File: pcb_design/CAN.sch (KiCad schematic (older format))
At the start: 5 parts

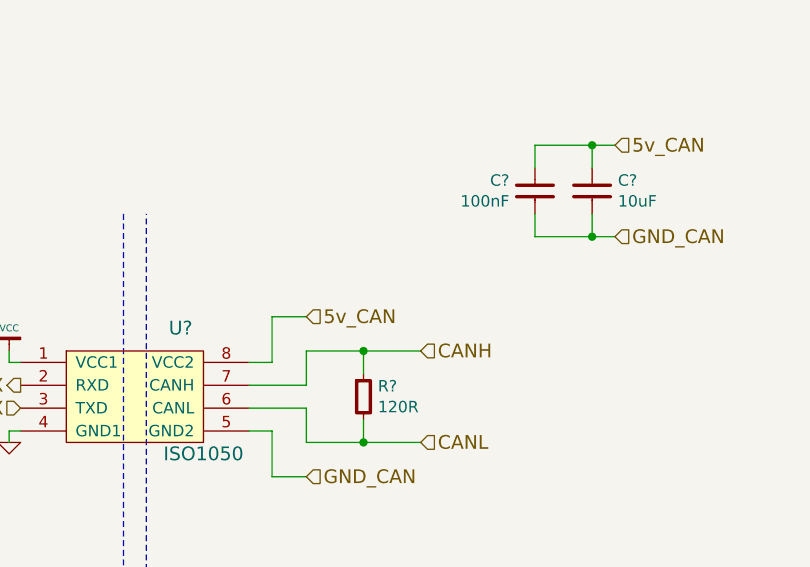
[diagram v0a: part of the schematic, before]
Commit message: Updated MCU sheet to comply with VESC 6 pinout. Added 5v analog inputs and updated some labels
Signed-off-by: Marcos Chaparro <mchaparro@paltatech.com>
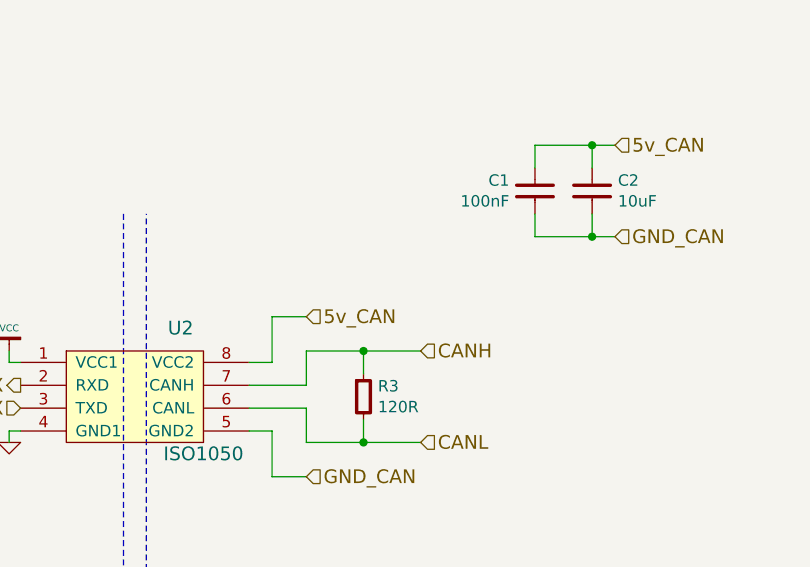
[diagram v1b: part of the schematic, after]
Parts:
- gave numbers to parts that had none: 4
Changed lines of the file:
@@
 $Descr A4 11693 8268
 encoding utf-8
-Sheet 3 10
+Sheet 3 12
 Title "BLDC Driver 4.11"
 Date "21 aug 2015"
@@
 $EndDescr
 $Comp
-L GND-RESCUE-BLDC_4 #PWR025
+L GND-RESCUE-BLDC_4 #PWR021
 U 1 1 53F59F97
 P 4950 4250
-F 0 "#PWR025" H 4950 4250 30  0001 C CNN
+F 0 "#PWR021" H 4950 4250 30  0001 C CNN
 F 1 "GND" H 4950 4180 30  0001 C CNN
 F 2 "" H 4950 4250 60  0000 C CNN
@@
 $EndComp
 $Comp
-L VCC #PWR026
+L VCC #PWR022
 U 1 1 53F59F9D
 P 4950 3850
-F 0 "#PWR026" H 4950 3950 30  0001 C CNN
+F 0 "#PWR022" H 4950 3950 30  0001 C CNN
 F 1 "VCC" H 4950 3950 30  0000 C CNN
 F 2 "" H 4950 3850 60  0001 C CNN
@@
 $EndComp
 $Comp
-L VCC #PWR027
+L VCC #PWR023
 U 1 1 53F59FAA
 P 4000 3850
-F 0 "#PWR027" H 4000 3950 30  0001 C CNN
+F 0 "#PWR023" H 4000 3950 30  0001 C CNN
 F 1 "VCC" H 4000 3950 30  0000 C CNN
 F 2 "" H 4000 3850 60  0001 C CNN
@@
 $EndComp
 $Comp
-L GND-RESCUE-BLDC_4 #PWR028
+L GND-RESCUE-BLDC_4 #PWR024
 U 1 1 53F59FB0
 P 4000 4250
-F 0 "#PWR028" H 4000 4250 30  0001 C CNN
+F 0 "#PWR024" H 4000 4250 30  0001 C CNN
 F 1 "GND" H 4000 4180 30  0001 C CNN
 F 2 "" H 4000 4250 60  0000 C CNN
@@
 CANL
 $Comp
-L ISO1050 U?
+L ISO1050 U2
 U 1 1 5886CCC8
 P 5500 4050
-F 0 "U?" H 5700 4350 60  0000 C CNN
+F 0 "U2" H 5700 4350 60  0000 C CNN
 F 1 "ISO1050" H 5800 3800 60  0000 C CNN
 F 2 "paltatech:SO8-ISO1050" H 5650 3850 60  0001 C CNN
@@
 $EndComp
 $Comp
-L R-0603 R?
+L R-0603 R3
 U 1 1 588777AE
 P 6500 4050
-F 0 "R?" H 6563 4096 50  0000 L CNN
+F 0 "R3" H 6563 4096 50  0000 L CNN
 F 1 "120R" H 6563 4005 50  0000 L CNN
 F 2 "IPC7351-Nominal:RESC1608X50" H 6500 4050 50  0001 C CNN
@@
 $EndComp
 $Comp
-L C-0805 C?
+L C-0805 C2
 U 1 1 58877A76
 P 7500 3150
-F 0 "C?" H 7613 3196 50  0000 L CNN
+F 0 "C2" H 7613 3196 50  0000 L CNN
 F 1 "10uF" H 7613 3105 50  0000 L CNN
 F 2 "IPC7351-Nominal:CAPC2012X70" H 7500 3150 50  0001 C CNN
@@
 $EndComp
 $Comp
-L C-0603 C?
+L C-0603 C1
 U 1 1 58877AC7
 P 7250 3150
-F 0 "C?" H 7362 3196 50  0000 L CNN
+F 0 "C1" H 7362 3196 50  0000 L CNN
 F 1 "100nF" H 7362 3105 50  0000 L CNN
 F 2 "IPC7351-Nominal:CAPC1608X55" H 7250 3150 50  0001 C CNN

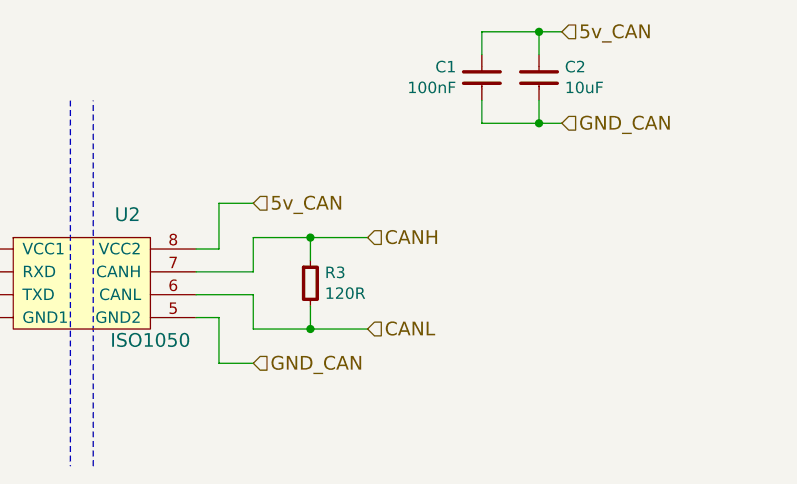
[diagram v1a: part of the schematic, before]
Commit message: Components placement, 3D models, updated some footprints to nominal IPC type
Signed-off-by: Marcos Chaparro <mchaparro@paltatech.com>
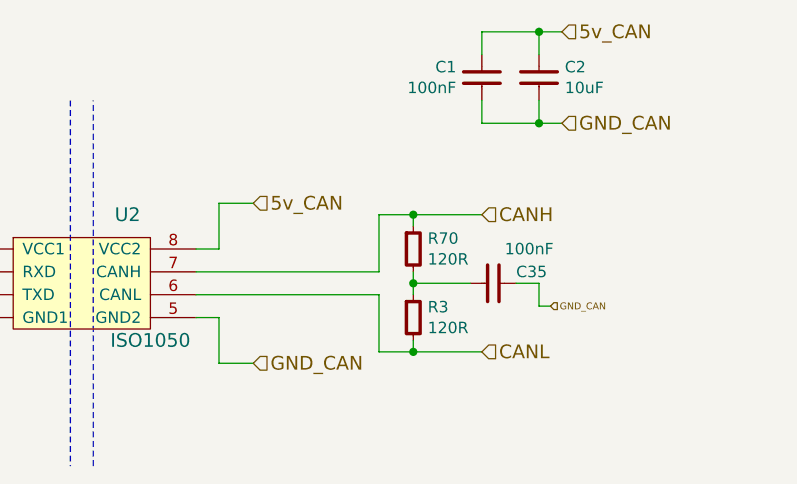
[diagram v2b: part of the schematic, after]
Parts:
- added C35: 100nF, IPC7351-Nominal:CAPC1608X55, symbol C-0603
- added R70: 120R, IPC7351-Nominal:RESC1608X50, symbol R-0603
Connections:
- net CANH: now also R70.1; no longer R3.1
- net GND_CAN: now also C35.1
- new net: C35.2, R3.1, R70.2
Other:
- moved on the sheet: R3
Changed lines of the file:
@@
 $EndDescr
 $Comp
-L GND-RESCUE-BLDC_4 #PWR021
+L GND-RESCUE-BLDC_4 #PWR21
 U 1 1 53F59F97
 P 4950 4250
-F 0 "#PWR021" H 4950 4250 30  0001 C CNN
+F 0 "#PWR21" H 4950 4250 30  0001 C CNN
 F 1 "GND" H 4950 4180 30  0001 C CNN
 F 2 "" H 4950 4250 60  0000 C CNN
@@
 $EndComp
 $Comp
-L VCC #PWR022
+L VCC #PWR20
 U 1 1 53F59F9D
 P 4950 3850
-F 0 "#PWR022" H 4950 3950 30  0001 C CNN
+F 0 "#PWR20" H 4950 3950 30  0001 C CNN
 F 1 "VCC" H 4950 3950 30  0000 C CNN
 F 2 "" H 4950 3850 60  0001 C CNN
@@
 $EndComp
 $Comp
-L VCC #PWR023
+L VCC #PWR18
 U 1 1 53F59FAA
 P 4000 3850
-F 0 "#PWR023" H 4000 3950 30  0001 C CNN
+F 0 "#PWR18" H 4000 3950 30  0001 C CNN
 F 1 "VCC" H 4000 3950 30  0000 C CNN
 F 2 "" H 4000 3850 60  0001 C CNN
@@
 $EndComp
 $Comp
-L GND-RESCUE-BLDC_4 #PWR024
+L GND-RESCUE-BLDC_4 #PWR19
 U 1 1 53F59FB0
 P 4000 4250
-F 0 "#PWR024" H 4000 4250 30  0001 C CNN
+F 0 "#PWR19" H 4000 4250 30  0001 C CNN
 F 1 "GND" H 4000 4180 30  0001 C CNN
 F 2 "" H 4000 4250 60  0000 C CNN
@@
 Text HLabel 5000 4100 0    60   Input ~ 0
 CAN_TX
-Text HLabel 6750 3850 2    60   Input ~ 0
+Text HLabel 7250 3750 2    60   Input ~ 0
 CANH
-Text HLabel 6750 4250 2    60   Input ~ 0
+Text HLabel 7250 4350 2    60   Input ~ 0
 CANL
 $Comp
@@
 L R-0603 R3
 U 1 1 588777AE
-P 6500 4050
-F 0 "R3" H 6563 4096 50  0000 L CNN
-F 1 "120R" H 6563 4005 50  0000 L CNN
-F 2 "IPC7351-Nominal:RESC1608X50" H 6500 4050 50  0001 C CNN
-F 3 "" H 6500 4100 60  0000 C CNN
-F 4 "RES SMD 1k 5% [0603]" H 7250 4600 60  0001 C CNN "BOM"
-	1    6500 4050
+P 6950 4200
+F 0 "R3" H 7013 4246 50  0000 L CNN
+F 1 "120R" H 7013 4155 50  0000 L CNN
+F 2 "IPC7351-Nominal:RESC1608X50" H 6950 4200 50  0001 C CNN
+F 3 "" H 6950 4250 60  0000 C CNN
+F 4 "RES SMD 1k 5% [0603]" H 7700 4750 60  0001 C CNN "BOM"
+	1    6950 4200
 	1    0    0    -1
 $EndComp
@@
 $EndComp
 Wire Wire Line
-	6250 4250 6750 4250
-Wire Wire Line
-	6250 4250 6250 4100
-Wire Wire Line
-	6250 4100 6000 4100
-Connection ~ 6500 4250
-Wire Wire Line
-	6000 4000 6250 4000
-Wire Wire Line
-	6250 4000 6250 3850
-Wire Wire Line
-	6250 3850 6750 3850
-Connection ~ 6500 3850
-Wire Wire Line
 	4950 3850 4950 3900
 Wire Wire Line
@@
 Wire Wire Line
 	4950 4200 5000 4200
-Wire Wire Line
-	6500 3950 6500 3850
-Wire Wire Line
-	6500 4150 6500 4250
 Wire Wire Line
 	7500 3050 7500 2950
@@
 Text Notes 1200 1700 0    300  ~ 60
 ISOLATED CAN BUS DRIVER
+$Comp
+L R-0603 R70
+U 1 1 588FD082
+P 6950 3900
+F 0 "R70" H 7013 3946 50  0000 L CNN
+F 1 "120R" H 7013 3855 50  0000 L CNN
+F 2 "IPC7351-Nominal:RESC1608X50" H 6950 3900 50  0001 C CNN
+F 3 "" H 6950 3950 60  0000 C CNN
+F 4 "RES SMD 1k 5% [0603]" H 7700 4450 60  0001 C CNN "BOM"
+	1    6950 3900
+	1    0    0    -1
+$EndComp
+Wire Wire Line
+	6000 4000 6800 4000
+Wire Wire Line
+	6800 4000 6800 3750
+Wire Wire Line
+	6800 3750 7250 3750
+Wire Wire Line
+	6950 3800 6950 3750
+Connection ~ 6950 3750
+$Comp
+L C-0603 C35
+U 1 1 588FD468
+P 7300 4050
+F 0 "C35" V 7350 4150 50  0000 L CNN
+F 1 "100nF" V 7450 4100 50  0000 L CNN
+F 2 "IPC7351-Nominal:CAPC1608X55" H 7300 4050 50  0001 C CNN
+F 3 "" H 7290 4025 60  0000 C CNN
+F 4 "CAP MLCC 100pF C0G 50V 5% [0603]" H 8100 4600 60  0001 C CNN "BOM"
+	1    7300 4050
+	0    1    -1   0
+$EndComp
+Wire Wire Line
+	7200 4050 6950 4050
+Wire Wire Line
+	6950 4000 6950 4100
+Connection ~ 6950 4050
+Wire Wire Line
+	6000 4100 6800 4100
+Wire Wire Line
+	6800 4100 6800 4350
+Wire Wire Line
+	6800 4350 7250 4350
+Wire Wire Line
+	6950 4350 6950 4300
+Connection ~ 6950 4350
+Wire Wire Line
+	7400 4050 7500 4050
+Wire Wire Line
+	7500 4050 7500 4150
+Text HLabel 7550 4150 2    30   Input ~ 0
+GND_CAN
+Wire Wire Line
+	7500 4150 7550 4150
 $EndSCHEMATC

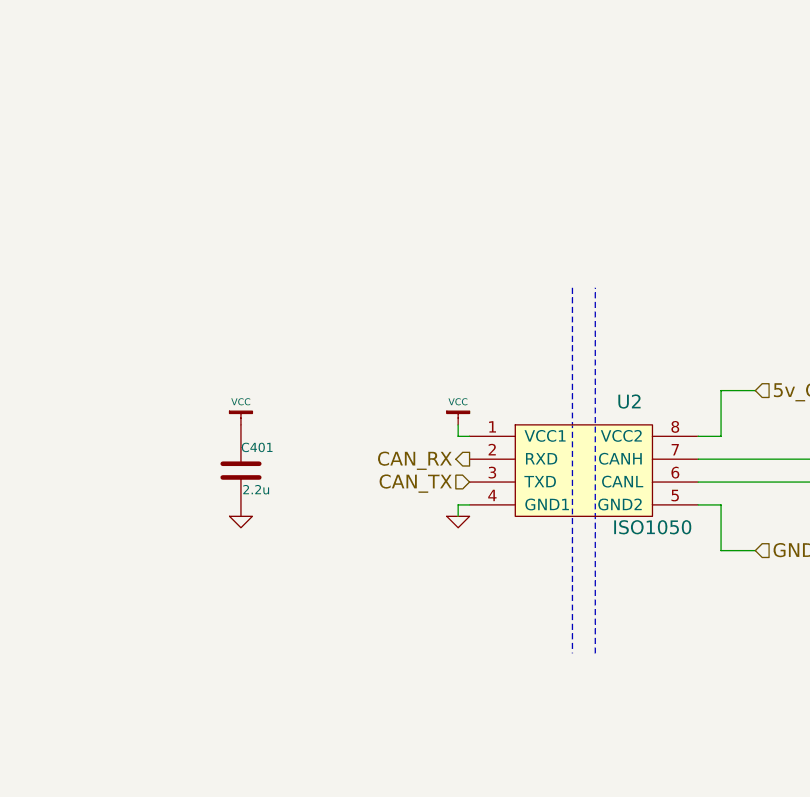
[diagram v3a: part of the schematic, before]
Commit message: Added lp filters, fuses, tvs and power symbols
Signed-off-by: Marcos Chaparro <mchaparro@paltatech.com>
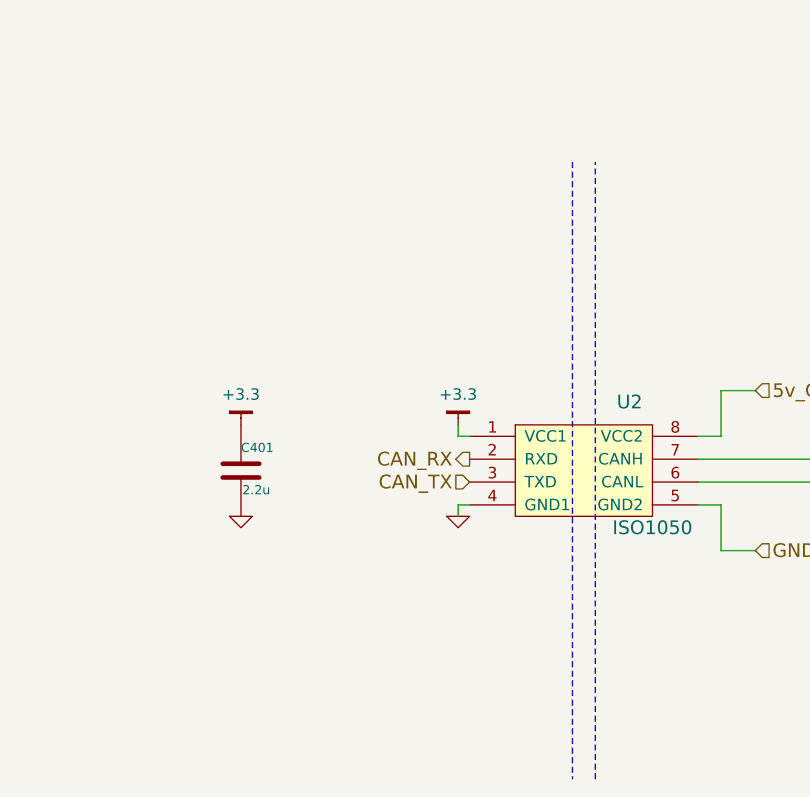
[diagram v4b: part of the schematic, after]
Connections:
- net VCC renamed +3.3
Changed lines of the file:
@@
-$EndComp
-$Comp
-L VCC #PWR23
-U 1 1 53F59F9D
-P 4950 3850
-F 0 "#PWR23" H 4950 3950 30  0001 C CNN
-F 1 "VCC" H 4950 3950 30  0000 C CNN
-F 2 "" H 4950 3850 60  0001 C CNN
-F 3 "" H 4950 3850 60  0001 C CNN
-	1    4950 3850
-	1    0    0    -1
 $EndComp
 $Comp
@@
 F 3 "" H 4000 4050 60  0000 C CNN
 	1    4000 4050
-	1    0    0    -1
-$EndComp
-$Comp
-L VCC #PWR21
-U 1 1 53F59FAA
-P 4000 3850
-F 0 "#PWR21" H 4000 3950 30  0001 C CNN
-F 1 "VCC" H 4000 3950 30  0000 C CNN
-F 2 "" H 4000 3850 60  0001 C CNN
-F 3 "" H 4000 3850 60  0001 C CNN
-	1    4000 3850
 	1    0    0    -1
 $EndComp
@@
 Wire Wire Line
 	6100 3900 6000 3900
-Wire Notes Line
-	5450 3250 5450 4850
-Wire Notes Line
-	5550 4850 5550 3250
 Text Notes 1200 1700 0    300  ~ 60
 ISOLATED CAN BUS DRIVER
@@
 Wire Wire Line
 	7500 4150 7550 4150
+$Comp
+L +3.3 #PWR?
+U 1 1 588B7BD5
+P 4000 3850
+F 0 "#PWR?" H 0   100 30  0001 C CNN
+F 1 "+3.3" H 4000 3983 50  0000 C CNN
+F 2 "" H 0   50  60  0000 C CNN
+F 3 "" H 0   50  60  0000 C CNN
+	1    4000 3850
+	1    0    0    -1
+$EndComp
+$Comp
+L +3.3 #PWR?
+U 1 1 588B7BFF
+P 4950 3850
+F 0 "#PWR?" H 0   100 30  0001 C CNN
+F 1 "+3.3" H 4950 3983 50  0000 C CNN
+F 2 "" H 0   50  60  0000 C CNN
+F 3 "" H 0   50  60  0000 C CNN
+	1    4950 3850
+	1    0    0    -1
+$EndComp
+Wire Notes Line
+	5450 2700 5450 5400
+Wire Notes Line
+	5550 5400 5550 2700
 $EndSCHEMATC
